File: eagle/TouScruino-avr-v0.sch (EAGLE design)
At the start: 53 parts, among them J1 AVR_ISP, Q1 8MHz, Q2 MMBT2222A, Q3 8MHz, U1 ATMEGA1284P, U2 AR1021, U3 MIC5209-3.3YS, U4 MCP73831, X2 USB-MICROB

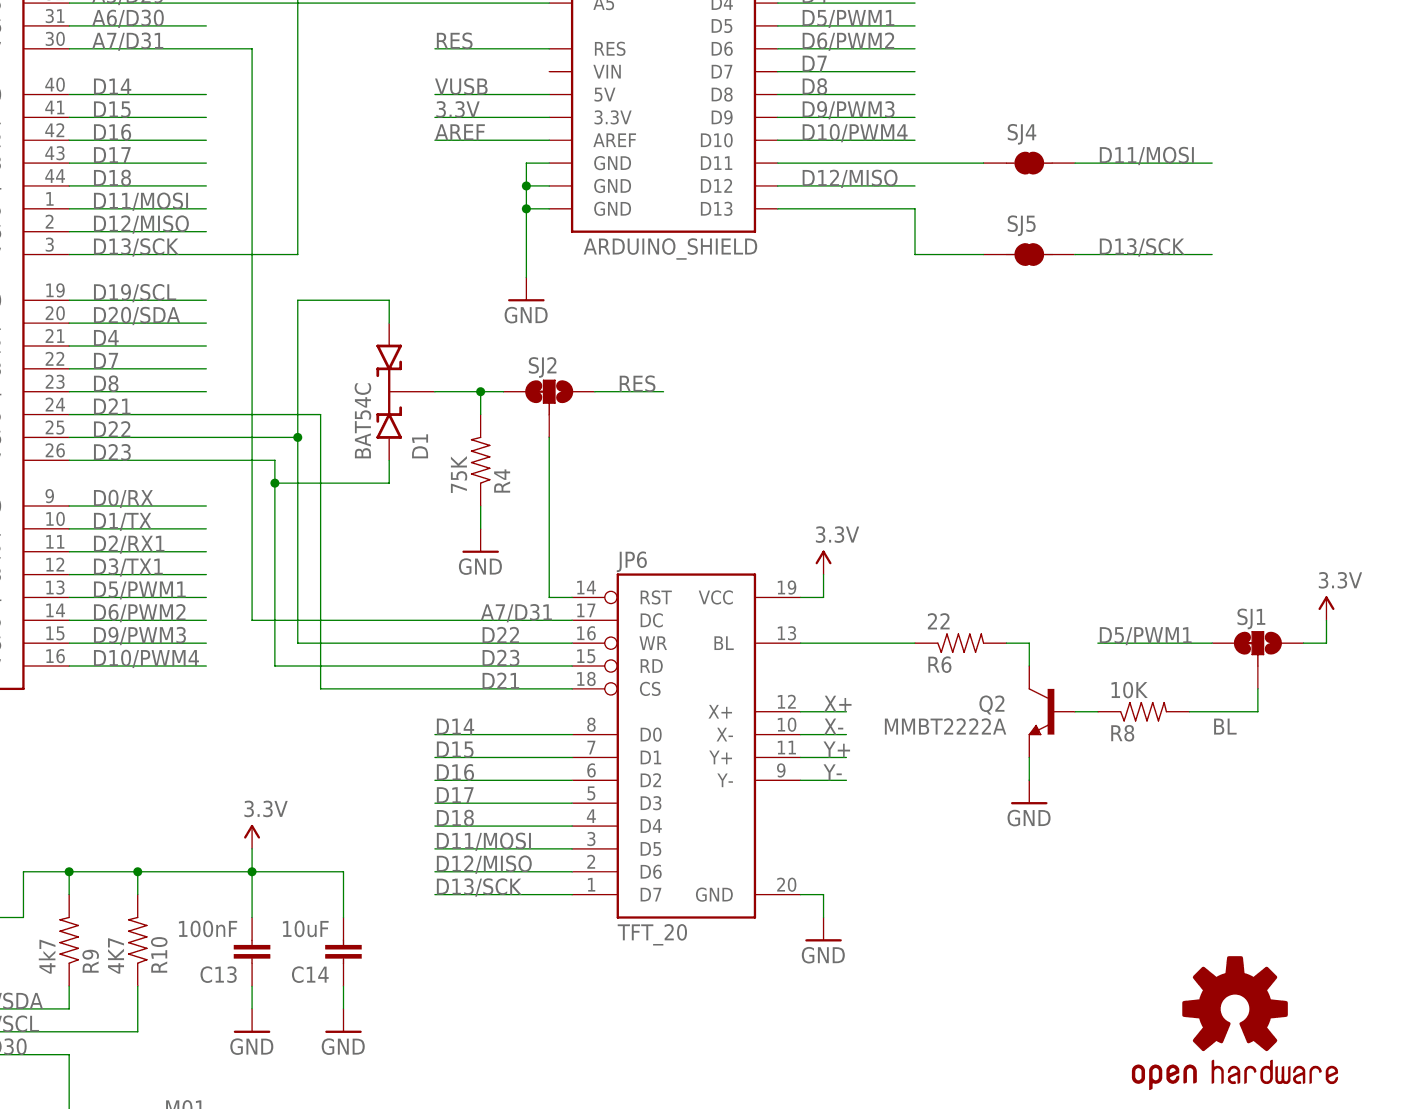
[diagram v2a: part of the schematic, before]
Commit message: 
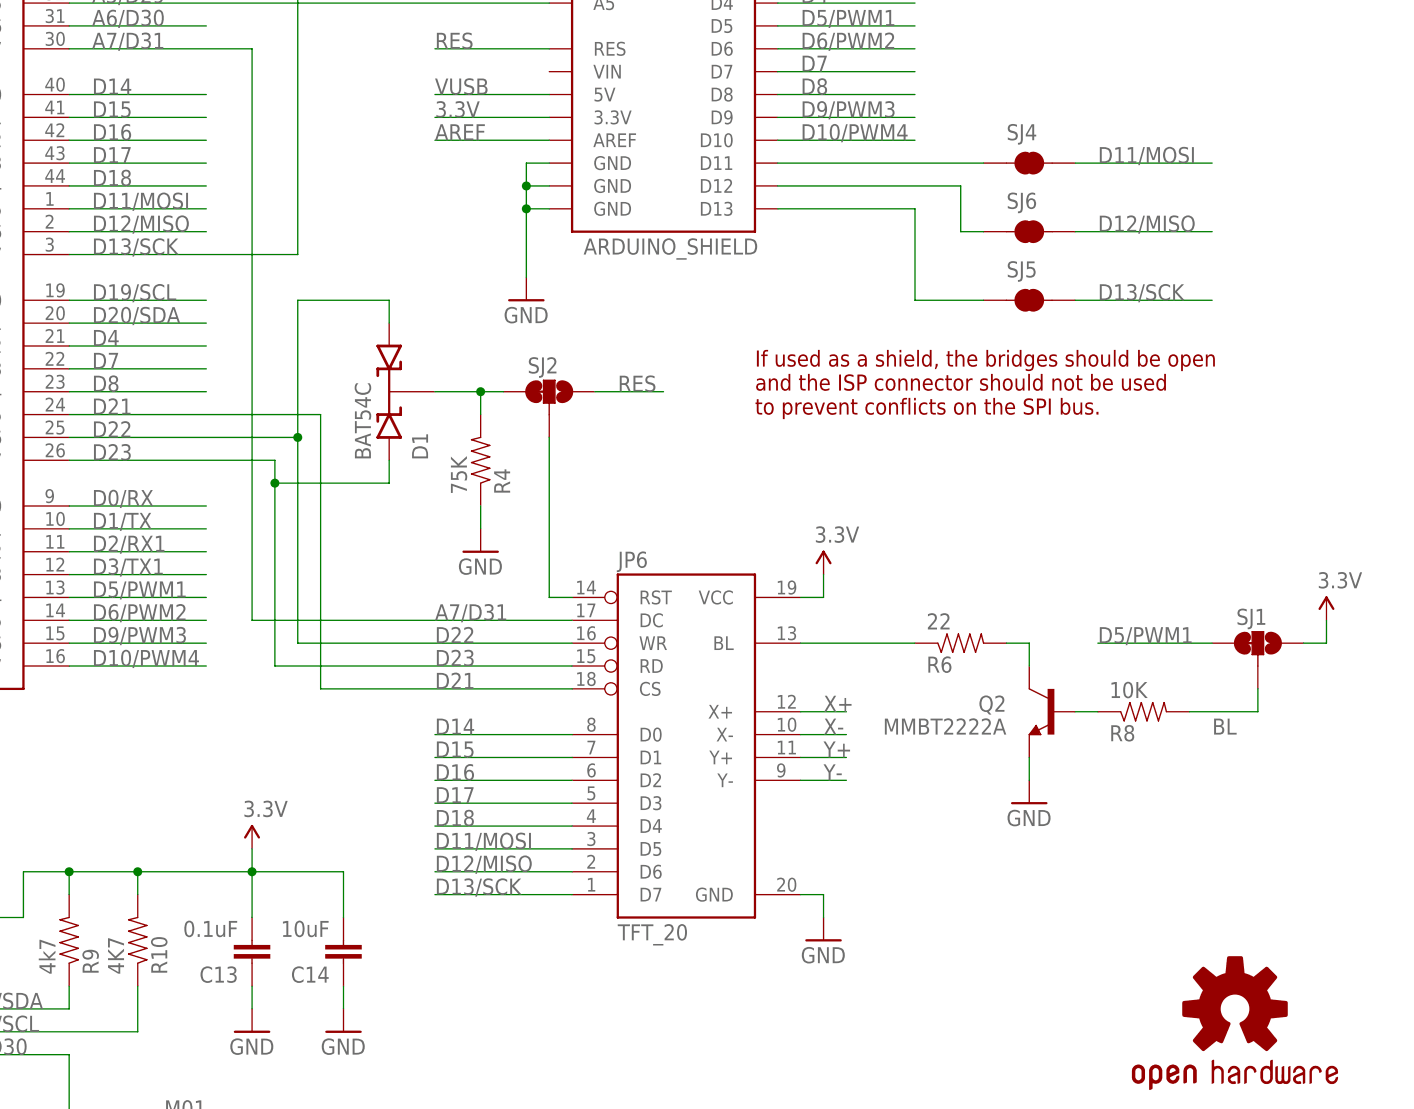
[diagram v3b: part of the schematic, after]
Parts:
- added SJ6: SOLDERJUMPERTRACE, SparkFun:SOLDERJUMPERTRACE
- C13: value 100nF -> 0.1uF
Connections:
- new net N$14: JP7.D12, SJ6.1
- net D12/MISO: now also SJ6.2; no longer JP7.D12
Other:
- note added: "If used as a shield, the bridges should be open and the ISP connector should not be used to prevent conflicts on the SPI bus."
- moved on the sheet: SJ5
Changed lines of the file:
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@@
 <part name="C11" library="SparkFun" deviceset="CAP" device="0805" value="10nF"/>
 <part name="C12" library="SparkFun" deviceset="CAP" device="0805" value="10nF"/>
-<part name="C13" library="SparkFun" deviceset="CAP" device="0805" value="100nF"/>
+<part name="C13" library="SparkFun" deviceset="CAP" device="0805" value="0.1uF"/>
 <part name="C14" library="SparkFun" deviceset="CAP" device="0805" value="10uF"/>
 <part name="SJ4" library="SparkFun" deviceset="SOLDERJUMPER" device="TRACE" value=""/>
@@
 <part name="JP8" library="wibauxl" deviceset="M01" device=""/>
 <part name="LED2" library="wibauxl" deviceset="LED" device="" value="Red"/>
+<part name="SJ6" library="SparkFun" deviceset="SOLDERJUMPER" device="TRACE" value=""/>
 </parts>
 <sheets>
@@
 <text x="243.84" y="-181.864" size="2.54" layer="94" ratio="12" rot="R180">http://code.google.com/p/ardurct</text>
 <wire x1="207.264" y1="127" x2="209.042" y2="127" width="0.4064" layer="94"/>
-<wire x1="207.264" y1="116.84" x2="209.042" y2="116.84" width="0.4064" layer="94"/>
+<wire x1="207.264" y1="111.76" x2="209.042" y2="111.76" width="0.4064" layer="94"/>
+<text x="177.8" y="99.06" size="1.778" layer="94">If used as a shield, the bridges should be open
+and the ISP connector should not be used
+to prevent conflicts on the SPI bus.</text>
+<wire x1="207.264" y1="119.38" x2="209.042" y2="119.38" width="0.4064" layer="94"/>
 </plain>
 <instances>
@@
 <instance part="C14" gate="G$1" x="132.08" y="40.64" rot="R180"/>
 <instance part="SJ4" gate="1" x="208.28" y="127"/>
-<instance part="SJ5" gate="1" x="208.28" y="116.84"/>
+<instance part="SJ5" gate="1" x="208.28" y="111.76"/>
 <instance part="JP6" gate="G$1" x="170.18" y="63.5"/>
 <instance part="R9" gate="G$1" x="101.6" y="40.64" rot="MR90"/>
@@
 <instance part="JP8" gate="G$1" x="114.3" y="17.78" rot="R180"/>
 <instance part="LED2" gate="G$1" x="147.32" y="175.26" rot="MR270"/>
+<instance part="SJ6" gate="1" x="208.28" y="119.38"/>
 </instances>
 <busses>
@@
 <pinref part="U1" gate="G$1" pin="(PCINT7/ADC7)PA7"/>
 <wire x1="121.92" y1="139.7" x2="121.92" y2="76.2" width="0.1524" layer="91"/>
-<label x="147.32" y="76.2" size="1.778" layer="95"/>
+<label x="142.24" y="76.2" size="1.778" layer="95"/>
 <pinref part="JP6" gate="G$1" pin="DC"/>
 <wire x1="157.48" y1="76.2" x2="121.92" y2="76.2" width="0.1524" layer="91"/>
@@
 </segment>
 <segment>
-<wire x1="180.34" y1="124.46" x2="195.58" y2="124.46" width="0.1524" layer="91"/>
-<label x="182.88" y="124.46" size="1.778" layer="95"/>
-<pinref part="JP7" gate="G$1" pin="D12"/>
+<pinref part="SJ6" gate="1" pin="2"/>
+<wire x1="213.36" y1="119.38" x2="228.6" y2="119.38" width="0.1524" layer="91"/>
+<label x="215.9" y="119.38" size="1.778" layer="95"/>
 </segment>
 <segment>
@@
 <net name="D13/SCK" class="0">
 <segment>
-<label x="215.9" y="116.84" size="1.778" layer="95"/>
+<label x="215.9" y="111.76" size="1.778" layer="95"/>
 <pinref part="SJ5" gate="1" pin="2"/>
-<wire x1="213.36" y1="116.84" x2="228.6" y2="116.84" width="0.1524" layer="91"/>
+<wire x1="213.36" y1="111.76" x2="228.6" y2="111.76" width="0.1524" layer="91"/>
 </segment>
 <segment>
@@
 <label x="104.14" y="93.98" size="1.778" layer="95"/>
 <pinref part="U1" gate="G$1" pin="(PCINT23/TOSC2)PC7"/>
-<label x="147.32" y="71.12" size="1.778" layer="95"/>
+<label x="142.24" y="71.12" size="1.778" layer="95"/>
 <pinref part="D1" gate="G$1" pin="A2"/>
 <wire x1="137.16" y1="91.44" x2="137.16" y2="93.98" width="0.1524" layer="91"/>
@@
 <label x="104.14" y="96.52" size="1.778" layer="95"/>
 <pinref part="U1" gate="G$1" pin="(PCINT22/TOSC1)PC6"/>
-<label x="147.32" y="73.66" size="1.778" layer="95"/>
+<label x="142.24" y="73.66" size="1.778" layer="95"/>
 <pinref part="D1" gate="G$1" pin="A1"/>
 <wire x1="137.16" y1="111.76" x2="137.16" y2="109.22" width="0.1524" layer="91"/>
@@
 <label x="104.14" y="99.06" size="1.778" layer="95"/>
 <pinref part="U1" gate="G$1" pin="(PCINT21/TDI)PC5"/>
-<label x="147.32" y="68.58" size="1.778" layer="95"/>
+<label x="142.24" y="68.58" size="1.778" layer="95"/>
 <pinref part="JP6" gate="G$1" pin="CS"/>
 <wire x1="129.54" y1="68.58" x2="157.48" y2="68.58" width="0.1524" layer="91"/>
@@
 <pinref part="JP7" gate="G$1" pin="D13"/>
 <wire x1="180.34" y1="121.92" x2="195.58" y2="121.92" width="0.1524" layer="91"/>
-<wire x1="195.58" y1="121.92" x2="195.58" y2="116.84" width="0.1524" layer="91"/>
+<wire x1="195.58" y1="121.92" x2="195.58" y2="111.76" width="0.1524" layer="91"/>
 <pinref part="SJ5" gate="1" pin="1"/>
-<wire x1="195.58" y1="116.84" x2="203.2" y2="116.84" width="0.1524" layer="91"/>
-</segment>
-</net>
+<wire x1="195.58" y1="111.76" x2="203.2" y2="111.76" width="0.1524" layer="91"/>
+</segment>
+</net>
+<net name="N$14" class="0">
+<segment>
+<pinref part="JP7" gate="G$1" pin="D12"/>
+<wire x1="180.34" y1="124.46" x2="200.66" y2="124.46" width="0.1524" layer="91"/>
+<wire x1="200.66" y1="124.46" x2="200.66" y2="119.38" width="0.1524" layer="91"/>
+<pinref part="SJ6" gate="1" pin="1"/>
+<wire x1="200.66" y1="119.38" x2="203.2" y2="119.38" width="0.1524" layer="91"/>
+</segment>
+</net>
